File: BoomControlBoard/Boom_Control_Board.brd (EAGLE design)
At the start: 50.8 x 50.8 mm, 28 parts, among them J1 Servo Header, J2 FTDI Header, U1 ATMEGA328P_TQFP, Y1 16MHz

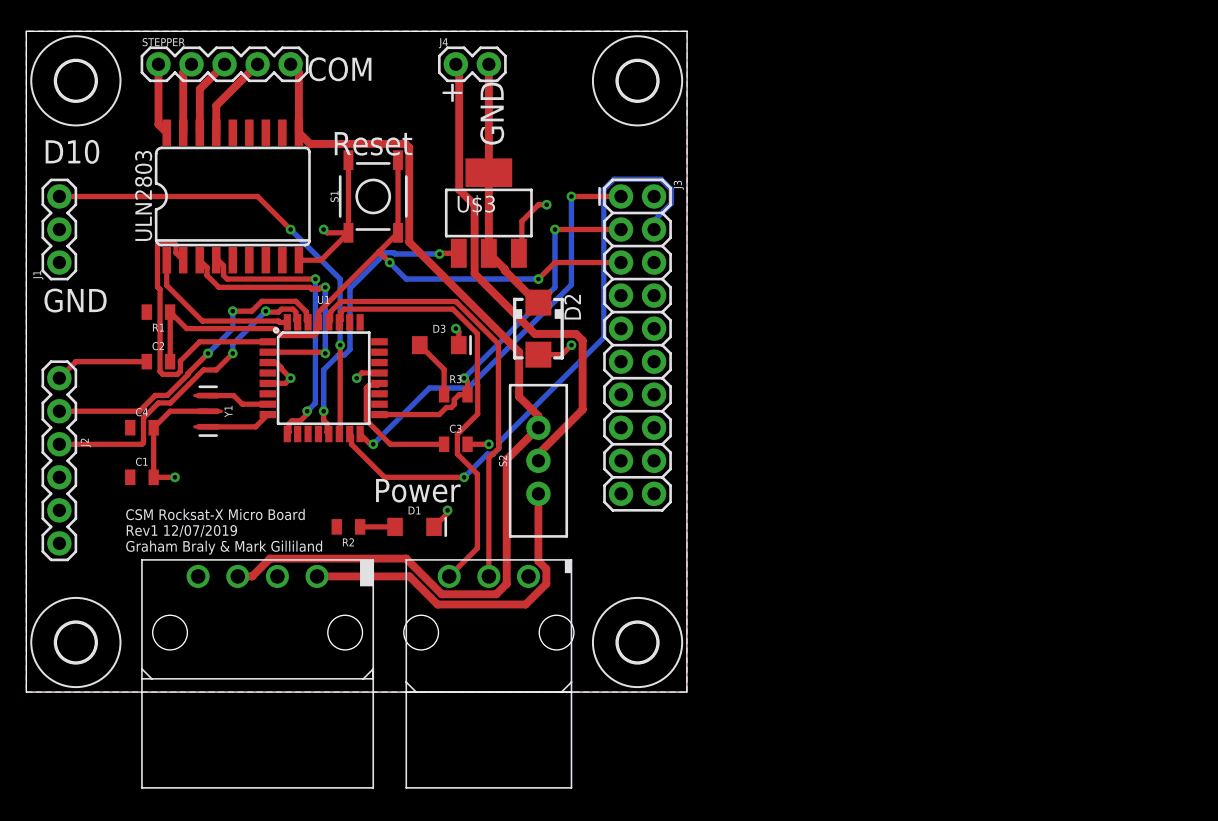
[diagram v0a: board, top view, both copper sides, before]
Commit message: Intial boom control board schematic and layout. Updated subystsem control board.
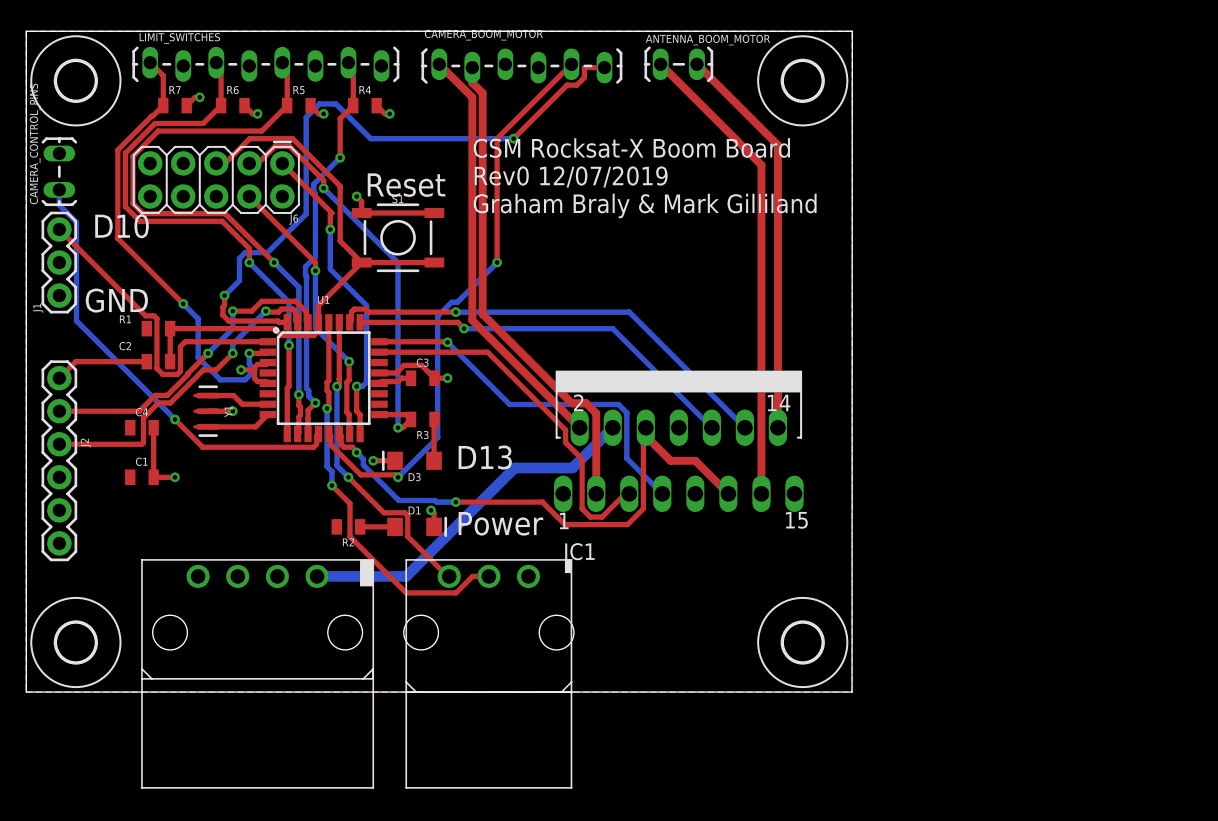
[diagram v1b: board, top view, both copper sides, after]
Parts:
- removed D2: S1M, diode:SMA
- removed J3: (no value), SparkFun-Connectors:2X10
- removed J4: (no value), SparkFun-Connectors:1X02
- removed S2: (no value), SparkFun-Switches:SWITCH_SPDT_PTH_11.6X4.0MM
- removed STEPPER: (no value), SparkFun-Connectors:1X05
- removed U$3: BUK9880-55A, PowerManagementParts:SOT223
- removed ULN2803: (no value), SparkFun-IC-Special-Function:SO18L
- added ANTENNA_BOOM_MOTOR, CAMERA_CONTROL_PINS: (no value), SparkFun-Connectors:1X02_LOCK_LONGPADS
- added CAMERA_BOOM_MOTOR: (no value), SparkFun-Connectors:1X06_LOCK_LONGPADS
- added IC1: L298, st-microelectronics:MULTIWATT-15
- added J6: (no value), SparkFun-Connectors:2X5
- added LIMIT_SWITCHES: (no value), SparkFun-Connectors:1X08_LOCK_LONGPADS
- added R4, R5, R6, R7: 10k, SparkFun-Resistors:0805
- moved H2 12.7 mm to (59.7, 3.81)
- moved H4 12.7 mm to (59.7, 47.0)
- moved D3 9.09 mm to (29.8, 17.8), turned to 180 degrees
- moved C3 5.68 mm to (30.5, 24.1)
- moved S1 3.70 mm to (28.6, 34.9), turned to 0 degrees
- moved R3 3.18 mm to (30.5, 21.0), turned to 180 degrees
- moved J1 2.54 mm to (2.54, 30.5)
- moved R1 1.27 mm to (10.2, 27.9)
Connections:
- removed net CH1_OUT: STEPPER.1, ULN2803.18
- removed net CH2_OUT: STEPPER.2, ULN2803.17
- removed net CH3_OUT: STEPPER.3, ULN2803.16
- removed net CH4_OUT: STEPPER.4, ULN2803.15
- removed net CH5_OUT: ULN2803.14
- removed net CH6_OUT: ULN2803.13
- removed net CH7_OUT: ULN2803.12
- removed net CH8_OUT: ULN2803.11
- removed net MOSFET_SWITCHED: D2.C, J4.2, U$3.2, U$3.4
- removed net N$1: J4.1, S2.2
- new net ANTENNA_+: ANTENNA_BOOM_MOTOR.1, IC1.13
- new net ANTENNA_-: ANTENNA_BOOM_MOTOR.2, IC1.14
- new net CAMERA_+: CAMERA_BOOM_MOTOR.1, IC1.2
- new net CAMERA_-: CAMERA_BOOM_MOTOR.2, IC1.3
- new net PB0: CAMERA_CONTROL_PINS.1, U1.12
- new net PC0: IC1.5, U1.23
- new net PC1: IC1.7, U1.24
- new net PC2: IC1.10, U1.25
- new net PC3: IC1.12, U1.26
- new net PD6: LIMIT_SWITCHES.5, R5.1, U1.10
- new net PD7: LIMIT_SWITCHES.7, R4.1, U1.11
- net 12V: now also IC1.4; no longer S2.3
- net 5V_ACT: no longer S2.1, STEPPER.5, ULN2803.10
- net GND: now also CAMERA_BOOM_MOTOR.3, CAMERA_CONTROL_PINS.2, IC1.8, J6.6, R4.2, R5.2, R6.2, R7.2; no longer D2.A, J3.6, U$3.3, ULN2803.9
- net MISO: now also J6.1; no longer J3.1
- net MOSI: now also J6.4; no longer J3.4
- net PB1: now also CAMERA_BOOM_MOTOR.5; no longer U$3.1
- net PB2: now also IC1.11, IC1.6; no longer J1.3
- net PD2: now also CAMERA_BOOM_MOTOR.6; no longer ULN2803.1
- net PD3: now also J1.3; no longer ULN2803.2
- net PD4: now also LIMIT_SWITCHES.1, R7.1; no longer ULN2803.3
- net PD5: now also LIMIT_SWITCHES.3, R6.1; no longer ULN2803.4
- net RESET: now also J6.5; no longer J3.5
- net SCK: now also J6.3; no longer J3.3
- net VCC: now also CAMERA_BOOM_MOTOR.4, IC1.9, J6.2, LIMIT_SWITCHES.2, LIMIT_SWITCHES.4, LIMIT_SWITCHES.6, LIMIT_SWITCHES.8; no longer J3.2
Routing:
- net 5V_ACT: track 75.8 -> 0.00 mm
- net PD6: track 0.00 -> 47.4 mm, vias 0 -> 2
- net PD2: track 12.4 -> 51.2 mm, vias 0 -> 2
- net N$1: track 37.8 -> 0.00 mm
- net CAMERA_-: track 0.00 -> 37.4 mm
- net ANTENNA_+: track 0.00 -> 36.2 mm
- net PC3: track 0.00 -> 35.0 mm, vias 0 -> 1
- net PB0: track 0.00 -> 34.1 mm, vias 0 -> 1
- net CAMERA_+: track 0.00 -> 32.4 mm
- net PD7: track 0.00 -> 31.4 mm, vias 0 -> 2
- net ANTENNA_-: track 0.00 -> 30.5 mm
- net PC2: track 0.00 -> 30.4 mm, vias 0 -> 1
- net PC1: track 0.00 -> 28.6 mm, vias 0 -> 1
- net PC0: track 0.00 -> 28.0 mm
- net MOSI: track 46.9 -> 21.6 mm, vias 1 -> 2
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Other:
- board size 50.8 x 50.8 mm -> 63.5 x 50.8 mm
- board text added: "CSM Rocksat-X Boom Board Rev0 12/07/2019 Graham Braly & Mark Gilliland"
- board text added: "D13"
- board text removed: "+"
- board text removed: "COM"
- board text removed: "CSM Rocksat-X Micro Board Rev1 12/07/2019 Graham Braly & Mark Gilliland"

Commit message: Added RF module to Boom Control Board.
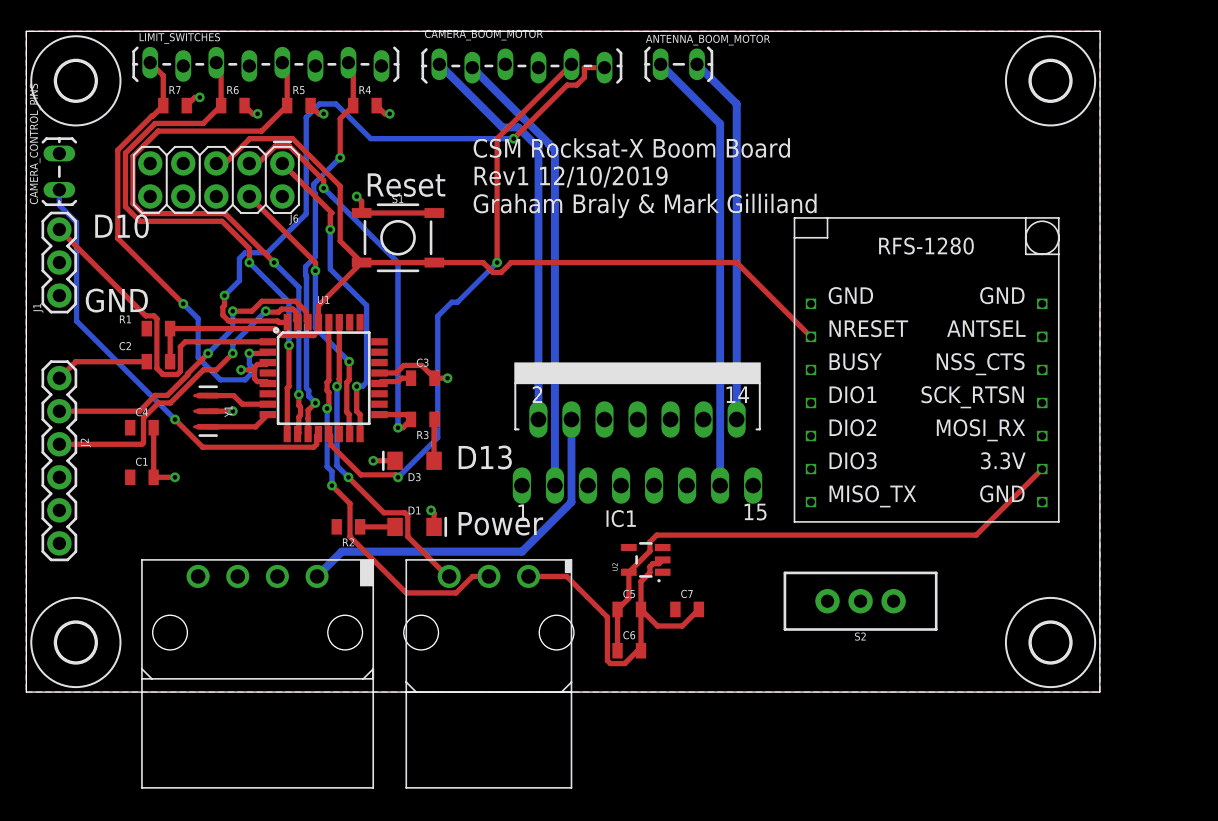
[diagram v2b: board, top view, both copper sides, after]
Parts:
- added C5, C7: 10uF, SparkFun-Capacitors:0805
- added C6: 0.1uF, SparkFun-Capacitors:0805
- added S2: (no value), SparkFun-Switches:SWITCH_SPDT_PTH_11.6X4.0MM
- added U$3: RFS1280_TH, PowerManagementParts:RFS1280-TH
- added U2: 3.3V/150mA, SparkFun-IC-Power:SOT23-5
- moved H2 19.0 mm to (78.7, 3.81)
- moved H4 19.0 mm to (78.7, 47.0)
- moved IC1 3.24 mm to (47.0, 23.5)
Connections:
- new net 3V3: C5.1, C6.1, S2.3, U$3.P$9, U2.5
- new net N$1: S2.2, U$3.P$13
- net GND: now also C5.2, C6.2, C7.2, S2.1, U$3.P$1, U$3.P$14, U$3.P$8, U2.2
- net MISO: now also U$3.P$7
- net MOSI: now also U$3.P$10
- net RESET: now also U$3.P$2
- net SCK: now also U$3.P$11
- net VCC: now also C7.1, U2.1, U2.3
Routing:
- net PB2: track 42.6 -> 0.00 mm, vias 2 -> 0
- net 3V3: track 0.00 -> 41.9 mm
- net PC3: track 35.0 -> 0.00 mm, vias 1 -> 0
- net RESET: track 45.4 -> 77.3 mm
- net PC2: track 30.4 -> 0.00 mm, vias 1 -> 0
- net PC1: track 28.6 -> 0.00 mm, vias 1 -> 0
- net PC0: track 28.0 -> 0.00 mm
- net GND: track 32.6 -> 59.9 mm
- net CAMERA_-: track 37.4 -> 34.8 mm
- net ANTENNA_-: track 30.5 -> 28.6 mm
- net ANTENNA_+: track 36.2 -> 34.3 mm
- net CAMERA_+: track 32.4 -> 31.2 mm
- net 12V: track 27.5 -> 28.3 mm
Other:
- board size 63.5 x 50.8 mm -> 82.5 x 50.8 mm
- board text added: "CSM Rocksat-X Boom Board Rev1 12/10/2019 Graham Braly & Mark Gilliland"
- board text removed: "CSM Rocksat-X Boom Board Rev0 12/07/2019 Graham Braly & Mark Gilliland"

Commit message: Finished routing Boom Control Board, added breakout points and labels. Swapped L298 for SMD part and swapped to dual SMD/TH RF Module footprint.
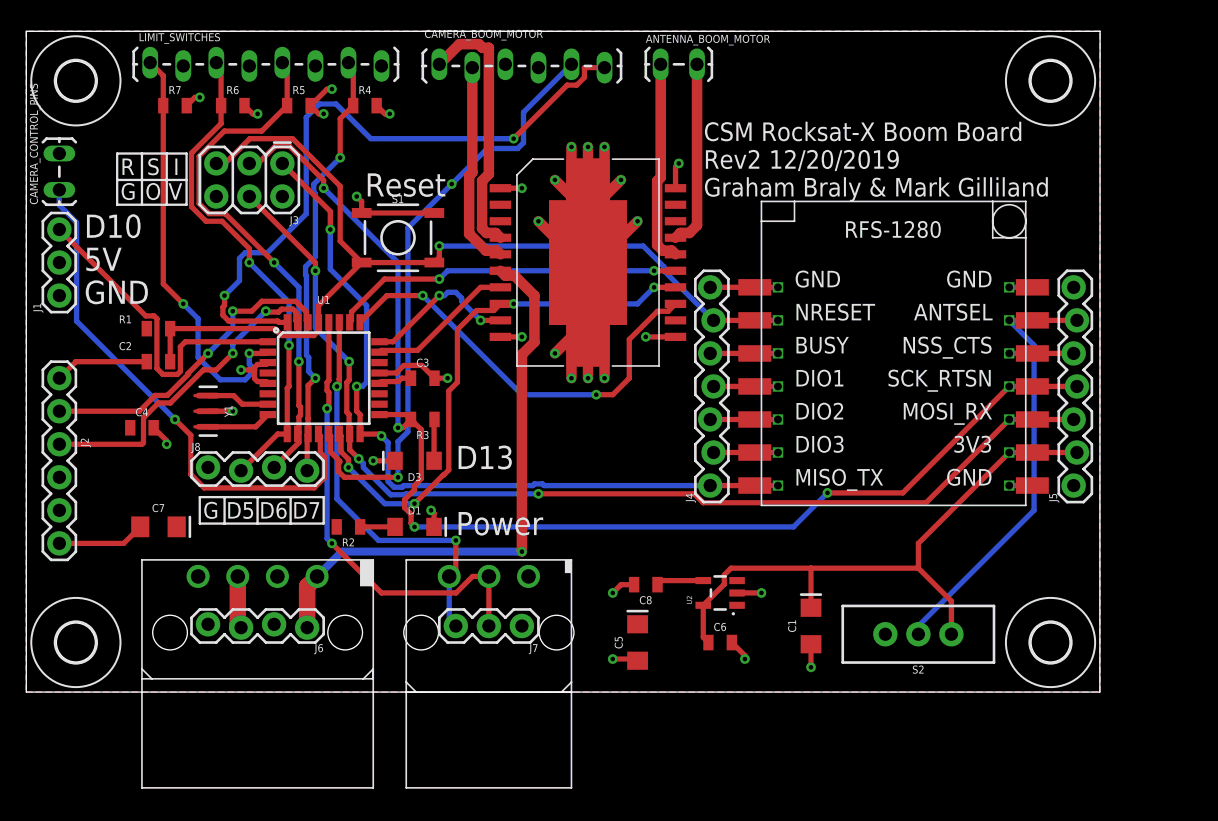
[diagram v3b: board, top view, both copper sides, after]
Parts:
- removed IC1: L298, st-microelectronics:MULTIWATT-15
- removed U$3: RFS1280_TH, PowerManagementParts:RFS1280-TH
- added C8: 470pF, SparkFun-Capacitors:0805
- added J3: (no value), SparkFun-Connectors:2X3
- added J4, J5: (no value), SparkFun-Connectors:1X07_LOCK
- added J7: 455-1750-1-ND, SparkFun-Connectors:1X03
- added J8: (no value), SparkFun-Connectors:1X04_LOCK
- added U$4: L298, SparkFun-IC-Special-Function:POWERSO20_L298_PAD
- added U$5: RFS-1280-1, PowerManagementParts:RFS-1280-1
- C1, C5, C7: device SparkFun-Capacitors:0805 -> SparkFun-Capacitors:EIA3216
- J6: device SparkFun-Connectors:2X5 -> SparkFun-Connectors:1X04_LOCK
- moved C1 52.7 mm to (60.3, 5.08), turned to 90 degrees
- moved C7 41.1 mm to (10.2, 12.7)
- moved J6 35.6 mm to (21.6, 5.08)
- moved C6 7.01 mm to (53.3, 3.81)
- moved U2 6.25 mm to (53.3, 7.62)
- moved S2 5.12 mm to (68.6, 4.45)
- moved C5 2.62 mm to (47.0, 3.81), turned to 90 degrees
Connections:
- removed net N$1: S2.2, U$3.P$13
- new net ANTSEL: J5.6, S2.2, U$5.P$13, U$5.P$27
- new net BUSY: J4.5, U$5.P$17, U$5.P$3
- new net CTS: J5.5, U$5.P$12, U$5.P$26
- new net DIO1: J4.4, U$5.P$18, U$5.P$4
- new net DIO2: J4.3, U$5.P$19, U$5.P$5
- new net DIO3: J4.2, U$5.P$20, U$5.P$6
- new net N$8: C8.1, U2.4
- net 12V: now also J6.1, U$4.6; no longer IC1.4
- net 3V3: now also C1.+, J5.2, U$5.P$23, U$5.P$9; no longer C5.1, U$3.P$9
- net 5V_ACT: now also J6.3
- net ANTENNA_+: now also U$4.16; no longer IC1.13
- net ANTENNA_-: now also U$4.17; no longer IC1.14
- net CAMERA_+: now also U$4.4; no longer IC1.2
- net CAMERA_-: now also U$4.5; no longer IC1.3
- net GND: now also C1.-, C5.-, C7.-, C8.2, J3.6, J4.7, J5.1, J5.7, J6.2, J7.1, J8.1, U$4.1, U$4.10, U$4.11, U$4.20, U$4.PAD, U$5.P$1, U$5.P$14, U$5.P$15, U$5.P$22, U$5.P$28, U$5.P$8; no longer C1.2, C5.2, C7.2, IC1.8, J6.6, U$3.P$1, U$3.P$14, U$3.P$8
- net MISO: now also J3.1, J4.1, U$5.P$21, U$5.P$7; no longer J6.1, U$3.P$7
- net MOSI: now also J3.4, J5.3, U$5.P$10, U$5.P$24; no longer J6.4, U$3.P$10
- net PB2: now also U$4.14, U$4.8; no longer IC1.11, IC1.6
- net PC0: now also U$4.7; no longer IC1.5
- net PC1: now also U$4.9; no longer IC1.7
- net PC2: now also U$4.13; no longer IC1.10
- net PC3: now also U$4.15; no longer IC1.12
- net PD5: now also J8.2
- net PD6: now also J8.3
- net PD7: now also J8.4
- net RESET: now also J3.5, J4.6, U$5.P$16, U$5.P$2; no longer J6.5, U$3.P$2
- net SCK: now also J3.3, J5.4, U$5.P$11, U$5.P$25; no longer J6.3, U$3.P$11
- net SCL: now also J7.2
- net SDA: now also J7.3
- net VCC: now also C5.+, C7.+, J3.2, J6.4, U$4.12; no longer C1.1, C7.1, IC1.9, J6.2
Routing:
- net GND: track 59.9 -> 151.6 mm, vias 11 -> 32
- net SCK: track 32.6 -> 97.4 mm, vias 2 -> 4
- net MOSI: track 21.6 -> 83.1 mm, vias 2 -> 4
- net PB2: track 0.00 -> 42.0 mm, vias 0 -> 4
- net MISO: track 24.3 -> 59.9 mm, vias 2 -> 3
- net ANTSEL: track 0.00 -> 33.8 mm
- net PC2: track 0.00 -> 32.9 mm, vias 0 -> 2
- net PC3: track 0.00 -> 27.1 mm, vias 0 -> 2
- net CAMERA_-: track 34.8 -> 15.9 mm
- net ANTENNA_+: track 34.3 -> 15.7 mm
- net 12V: track 28.3 -> 44.3 mm, vias 0 -> 1
- net ANTENNA_-: track 28.6 -> 14.4 mm
- net PC1: track 0.00 -> 11.9 mm, vias 0 -> 2
- net PC0: track 0.00 -> 11.4 mm
- net CAMERA_+: track 31.2 -> 20.4 mm
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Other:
- board text added: "5V"
- board text added: "CSM Rocksat-X Boom Board Rev2 12/20/2019 Graham Braly & Mark Gilliland"
- board text added: "D5"
- board text added: "D6"
- board text added: "D7"
- board text added: "G"
- board text added: "I"
- board text added: "O"
- board text added: "R"
- board text added: "S"
- board text added: "V"
- board text removed: "CSM Rocksat-X Boom Board Rev1 12/10/2019 Graham Braly & Mark Gilliland"
